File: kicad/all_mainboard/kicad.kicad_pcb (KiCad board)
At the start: 2 copper layers, 266 x 95 mm, 133 parts

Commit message: added kicad files
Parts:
- added D1: D,Zener,IEC, Diode_THT:D_DO-41_SOD81_P10.16mm_Horizontal, B.Cu at (127.4, 57.0)
- added D2: D,Zener,IEC, Diode_THT:D_DO-41_SOD81_P10.16mm_Horizontal, B.Cu at (131.4, 60.5)
- added J1: USB_A, custom:PinHeader_1x04_P2.00mm_Horizontal, F.Cu at (131.5, 26.0)
- added R1: 68R, Diode_THT:D_DO-41_SOD81_P10.16mm_Horizontal, B.Cu at (128.0, 84.4)
- added R2: 68R, Diode_THT:D_DO-41_SOD81_P10.16mm_Horizontal, B.Cu at (130.5, 71.4)
- added R3: 1k5, Diode_THT:D_DO-41_SOD81_P10.16mm_Horizontal, B.Cu at (111.5, 81.4)
- moved A2 157.4 mm to (122.9, 108.1), turned to -90 degrees
- moved D-2-13 25.3 mm to (266.7, 54.5), turned to 0 degrees
- moved D-4-6 9.79 mm to (141.0, 96.7), turned to -90 degrees
- moved D-0-10 8.24 mm to (209.7, 25.9), turned to 0 degrees
- moved D-0-11 8.24 mm to (228.7, 25.9), turned to 0 degrees
- moved D-0-12 8.24 mm to (247.7, 25.9), turned to 0 degrees
- moved D-0-13 8.24 mm to (266.7, 25.9), turned to 0 degrees
- moved D-0-2 8.24 mm to (57.7, 25.9), turned to 0 degrees
- moved D-0-3 8.24 mm to (76.7, 25.9), turned to 0 degrees
- moved D-0-4 8.24 mm to (95.7, 25.9), turned to 0 degrees
- moved D-0-5 8.24 mm to (114.7, 25.9), turned to 0 degrees
- moved D-0-7 8.24 mm to (152.7, 25.9), turned to 0 degrees
- moved D-0-8 8.24 mm to (171.7, 25.9), turned to 0 degrees
- moved D-0-9 8.24 mm to (190.7, 25.9), turned to 0 degrees
- moved D-1-10 8.24 mm to (209.7, 44.9), turned to 0 degrees
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- renumbered D-4-5 to D-4-6, D-4-8 to D-4-7, SW-4-5 to SW-4-6, SW-4-8 to SW-4-7
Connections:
- A2 pad A0: unconnected-(A2-PadA0) -> /tiny+ switch array standard/wr-4
- A2 pad A1: /tiny+ switch array standard/r-13 -> /tiny+ switch array standard/r-4
- A2 pad A2: /tiny+ switch array standard/r-12 -> /tiny+ switch array standard/r-0
- A2 pad A3: /tiny+ switch array standard/r-11 -> /tiny+ switch array standard/r-1
- A2 pad A4: /tiny+ switch array standard/r-10 -> /tiny+ switch array standard/r-3
- A2 pad A5: /tiny+ switch array standard/r-9 -> /tiny+ switch array standard/r-2
- A2 pad A6: /tiny+ switch array standard/r-8 -> /tiny+ switch array standard/r-9
- A2 pad A7: /tiny+ switch array standard/r-7 -> /tiny+ switch array standard/r-10
- A2 pad D1: /tiny+ switch array standard/r-6 -> /tiny+ switch array standard/wr-0
- A2 pad D10: /tiny+ switch array standard/wr-1 -> /tiny+ switch array standard/r-11
- A2 pad D11: /tiny+ switch array standard/wr-2 -> /tiny+ switch array standard/r-12
- A2 pad D12: /tiny+ switch array standard/wr-3 -> /tiny+ switch array standard/r-13
- A2 pad D13: /tiny+ switch array standard/wr-4 -> unconnected-(A2-D13_SCK-PadD13)
- A2 pad D2: unconnected-(A2-D2_INT0-PadD2) -> /tiny+ switch array standard/wr-1
- A2 pad D3: /tiny+ switch array standard/r-4 -> Net-(A2-D3_INT1)
- A2 pad D4: unconnected-(A2-PadD4) -> Net-(A2-PadD4)
- A2 pad D5: /tiny+ switch array standard/r-3 -> /tiny+ switch array standard/wr-3
- A2 pad D6: /tiny+ switch array standard/r-2 -> /tiny+ switch array standard/r-6
- A2 pad D7: /tiny+ switch array standard/r-1 -> /tiny+ switch array standard/wr-2
- A2 pad D8: /tiny+ switch array standard/r-0 -> /tiny+ switch array standard/r-7
- A2 pad D9: /tiny+ switch array standard/wr-0 -> /tiny+ switch array standard/r-8
- A2 pad GND1: unconnected-(A2-GND-PadGND1) -> Net-(D1-A+)
- A2 pad Vcc1: unconnected-(A2-Vcc-PadVcc1) -> Net-(A2-Vcc)
- D-4-6 pad 1: /tiny+ switch array standard/r-5 -> /tiny+ switch array standard/r-6
- D-4-6 pad 2: Net-(D-4-5-A) -> Net-(D-4-6-A)
- D-4-7 pad 1: /tiny+ switch array standard/r-8 -> /tiny+ switch array standard/r-7
- D-4-7 pad 2: Net-(D-4-8-A) -> Net-(D-4-7-A)
- SW-0-0 pad 1: /tiny+ switch array standard/wr-0 -> Net-(D-0-0-A)
- SW-0-0 pad 2: Net-(D-0-0-A) -> /tiny+ switch array standard/wr-0
- SW-0-1 pad 1: /tiny+ switch array standard/wr-0 -> Net-(D-0-1-A)
- SW-0-1 pad 2: Net-(D-0-1-A) -> /tiny+ switch array standard/wr-0
- SW-0-10 pad 1: /tiny+ switch array standard/wr-0 -> Net-(D-0-10-A)
- SW-0-10 pad 2: Net-(D-0-10-A) -> /tiny+ switch array standard/wr-0
- SW-0-11 pad 1: /tiny+ switch array standard/wr-0 -> Net-(D-0-11-A)
- SW-0-11 pad 2: Net-(D-0-11-A) -> /tiny+ switch array standard/wr-0
- SW-0-12 pad 1: /tiny+ switch array standard/wr-0 -> Net-(D-0-12-A)
- SW-0-12 pad 2: Net-(D-0-12-A) -> /tiny+ switch array standard/wr-0
- SW-0-13 pad 1: /tiny+ switch array standard/wr-0 -> Net-(D-0-13-A)
- SW-0-13 pad 2: Net-(D-0-13-A) -> /tiny+ switch array standard/wr-0
- SW-0-2 pad 1: /tiny+ switch array standard/wr-0 -> Net-(D-0-2-A)
- SW-0-2 pad 2: Net-(D-0-2-A) -> /tiny+ switch array standard/wr-0
- SW-0-3 pad 1: /tiny+ switch array standard/wr-0 -> Net-(D-0-3-A)
- SW-0-3 pad 2: Net-(D-0-3-A) -> /tiny+ switch array standard/wr-0
- SW-0-4 pad 1: /tiny+ switch array standard/wr-0 -> Net-(D-0-4-A)
- SW-0-4 pad 2: Net-(D-0-4-A) -> /tiny+ switch array standard/wr-0
- SW-0-5 pad 1: /tiny+ switch array standard/wr-0 -> Net-(D-0-5-A)
- SW-0-5 pad 2: Net-(D-0-5-A) -> /tiny+ switch array standard/wr-0
- SW-0-6 pad 1: /tiny+ switch array standard/wr-0 -> Net-(D-0-6-A)
- SW-0-6 pad 2: Net-(D-0-6-A) -> /tiny+ switch array standard/wr-0
- SW-0-7 pad 1: /tiny+ switch array standard/wr-0 -> Net-(D-0-7-A)
- SW-0-7 pad 2: Net-(D-0-7-A) -> /tiny+ switch array standard/wr-0
- SW-0-8 pad 1: /tiny+ switch array standard/wr-0 -> Net-(D-0-8-A)
- SW-0-8 pad 2: Net-(D-0-8-A) -> /tiny+ switch array standard/wr-0
- SW-0-9 pad 1: /tiny+ switch array standard/wr-0 -> Net-(D-0-9-A)
- SW-0-9 pad 2: Net-(D-0-9-A) -> /tiny+ switch array standard/wr-0
- SW-1-0 pad 1: /tiny+ switch array standard/wr-1 -> Net-(D-1-0-A)
- SW-1-0 pad 2: Net-(D-1-0-A) -> /tiny+ switch array standard/wr-1
- SW-1-1 pad 1: /tiny+ switch array standard/wr-1 -> Net-(D-1-1-A)
- SW-1-1 pad 2: Net-(D-1-1-A) -> /tiny+ switch array standard/wr-1
- SW-1-10 pad 1: /tiny+ switch array standard/wr-1 -> Net-(D-1-10-A)
- SW-1-10 pad 2: Net-(D-1-10-A) -> /tiny+ switch array standard/wr-1
- SW-1-11 pad 1: /tiny+ switch array standard/wr-1 -> Net-(D-1-11-A)
- SW-1-11 pad 2: Net-(D-1-11-A) -> /tiny+ switch array standard/wr-1
- SW-1-12 pad 1: /tiny+ switch array standard/wr-1 -> Net-(D-1-12-A)
- SW-1-12 pad 2: Net-(D-1-12-A) -> /tiny+ switch array standard/wr-1
- SW-1-2 pad 1: /tiny+ switch array standard/wr-1 -> Net-(D-1-2-A)
- SW-1-2 pad 2: Net-(D-1-2-A) -> /tiny+ switch array standard/wr-1
- SW-1-3 pad 1: /tiny+ switch array standard/wr-1 -> Net-(D-1-3-A)
- SW-1-3 pad 2: Net-(D-1-3-A) -> /tiny+ switch array standard/wr-1
- SW-1-4 pad 1: /tiny+ switch array standard/wr-1 -> Net-(D-1-4-A)
- SW-1-4 pad 2: Net-(D-1-4-A) -> /tiny+ switch array standard/wr-1
- SW-1-5 pad 1: /tiny+ switch array standard/wr-1 -> Net-(D-1-5-A)
- SW-1-5 pad 2: Net-(D-1-5-A) -> /tiny+ switch array standard/wr-1
- SW-1-6 pad 1: /tiny+ switch array standard/wr-1 -> Net-(D-1-6-A)
- SW-1-6 pad 2: Net-(D-1-6-A) -> /tiny+ switch array standard/wr-1
- SW-1-7 pad 1: /tiny+ switch array standard/wr-1 -> Net-(D-1-7-A)
- SW-1-7 pad 2: Net-(D-1-7-A) -> /tiny+ switch array standard/wr-1
- SW-1-8 pad 1: /tiny+ switch array standard/wr-1 -> Net-(D-1-8-A)
- SW-1-8 pad 2: Net-(D-1-8-A) -> /tiny+ switch array standard/wr-1
- SW-1-9 pad 1: /tiny+ switch array standard/wr-1 -> Net-(D-1-9-A)
- SW-1-9 pad 2: Net-(D-1-9-A) -> /tiny+ switch array standard/wr-1
- SW-2-0 pad 1: /tiny+ switch array standard/wr-2 -> Net-(D-2-0-A)
- SW-2-0 pad 2: Net-(D-2-0-A) -> /tiny+ switch array standard/wr-2
- SW-2-1 pad 1: /tiny+ switch array standard/wr-2 -> Net-(D-2-1-A)
- SW-2-1 pad 2: Net-(D-2-1-A) -> /tiny+ switch array standard/wr-2
- SW-2-10 pad 1: /tiny+ switch array standard/wr-2 -> Net-(D-2-10-A)
- SW-2-10 pad 2: Net-(D-2-10-A) -> /tiny+ switch array standard/wr-2
- SW-2-11 pad 1: /tiny+ switch array standard/wr-2 -> Net-(D-2-11-A)
- SW-2-11 pad 2: Net-(D-2-11-A) -> /tiny+ switch array standard/wr-2
- SW-2-12 pad 1: /tiny+ switch array standard/wr-2 -> Net-(D-2-12-A)
- SW-2-12 pad 2: Net-(D-2-12-A) -> /tiny+ switch array standard/wr-2
- SW-2-13 pad 1: /tiny+ switch array standard/wr-2 -> Net-(D-2-13-A)
- SW-2-13 pad 2: Net-(D-2-13-A) -> /tiny+ switch array standard/wr-2
- SW-2-2 pad 1: /tiny+ switch array standard/wr-2 -> Net-(D-2-2-A)
- SW-2-2 pad 2: Net-(D-2-2-A) -> /tiny+ switch array standard/wr-2
- SW-2-3 pad 1: /tiny+ switch array standard/wr-2 -> Net-(D-2-3-A)
- SW-2-3 pad 2: Net-(D-2-3-A) -> /tiny+ switch array standard/wr-2
- SW-2-4 pad 1: /tiny+ switch array standard/wr-2 -> Net-(D-2-4-A)
- SW-2-4 pad 2: Net-(D-2-4-A) -> /tiny+ switch array standard/wr-2
- SW-2-5 pad 1: /tiny+ switch array standard/wr-2 -> Net-(D-2-5-A)
- SW-2-5 pad 2: Net-(D-2-5-A) -> /tiny+ switch array standard/wr-2
- SW-2-6 pad 1: /tiny+ switch array standard/wr-2 -> Net-(D-2-6-A)
- SW-2-6 pad 2: Net-(D-2-6-A) -> /tiny+ switch array standard/wr-2
- SW-2-7 pad 1: /tiny+ switch array standard/wr-2 -> Net-(D-2-7-A)
- SW-2-7 pad 2: Net-(D-2-7-A) -> /tiny+ switch array standard/wr-2
- SW-2-8 pad 1: /tiny+ switch array standard/wr-2 -> Net-(D-2-8-A)
- SW-2-8 pad 2: Net-(D-2-8-A) -> /tiny+ switch array standard/wr-2
- SW-2-9 pad 1: /tiny+ switch array standard/wr-2 -> Net-(D-2-9-A)
- SW-2-9 pad 2: Net-(D-2-9-A) -> /tiny+ switch array standard/wr-2
- SW-3-0 pad 1: /tiny+ switch array standard/wr-3 -> Net-(D-3-0-A)
- SW-3-0 pad 2: Net-(D-3-0-A) -> /tiny+ switch array standard/wr-3
- SW-3-1 pad 1: /tiny+ switch array standard/wr-3 -> Net-(D-3-1-A)
- SW-3-1 pad 2: Net-(D-3-1-A) -> /tiny+ switch array standard/wr-3
- SW-3-10 pad 1: /tiny+ switch array standard/wr-3 -> Net-(D-3-10-A)
- SW-3-10 pad 2: Net-(D-3-10-A) -> /tiny+ switch array standard/wr-3
- SW-3-11 pad 1: /tiny+ switch array standard/wr-3 -> Net-(D-3-11-A)
- SW-3-11 pad 2: Net-(D-3-11-A) -> /tiny+ switch array standard/wr-3
- SW-3-12 pad 1: /tiny+ switch array standard/wr-3 -> Net-(D-3-12-A)
- SW-3-12 pad 2: Net-(D-3-12-A) -> /tiny+ switch array standard/wr-3
- SW-3-13 pad 1: /tiny+ switch array standard/wr-3 -> Net-(D-3-13-A)
- SW-3-13 pad 2: Net-(D-3-13-A) -> /tiny+ switch array standard/wr-3
- SW-3-2 pad 1: /tiny+ switch array standard/wr-3 -> Net-(D-3-2-A)
- SW-3-2 pad 2: Net-(D-3-2-A) -> /tiny+ switch array standard/wr-3
- SW-3-3 pad 1: /tiny+ switch array standard/wr-3 -> Net-(D-3-3-A)
- SW-3-3 pad 2: Net-(D-3-3-A) -> /tiny+ switch array standard/wr-3
- SW-3-4 pad 1: /tiny+ switch array standard/wr-3 -> Net-(D-3-4-A)
- SW-3-4 pad 2: Net-(D-3-4-A) -> /tiny+ switch array standard/wr-3
- SW-3-5 pad 1: /tiny+ switch array standard/wr-3 -> Net-(D-3-5-A)
- SW-3-5 pad 2: Net-(D-3-5-A) -> /tiny+ switch array standard/wr-3
- SW-3-6 pad 1: /tiny+ switch array standard/wr-3 -> Net-(D-3-6-A)
- SW-3-6 pad 2: Net-(D-3-6-A) -> /tiny+ switch array standard/wr-3
- SW-3-7 pad 1: /tiny+ switch array standard/wr-3 -> Net-(D-3-7-A)
- SW-3-7 pad 2: Net-(D-3-7-A) -> /tiny+ switch array standard/wr-3
- SW-3-8 pad 1: /tiny+ switch array standard/wr-3 -> Net-(D-3-8-A)
- SW-3-8 pad 2: Net-(D-3-8-A) -> /tiny+ switch array standard/wr-3
- SW-3-9 pad 1: /tiny+ switch array standard/wr-3 -> Net-(D-3-9-A)
- SW-3-9 pad 2: Net-(D-3-9-A) -> /tiny+ switch array standard/wr-3
- SW-4-0 pad 1: /tiny+ switch array standard/wr-4 -> Net-(D-4-0-A)
- SW-4-0 pad 2: Net-(D-4-0-A) -> /tiny+ switch array standard/wr-4
- SW-4-1 pad 1: /tiny+ switch array standard/wr-4 -> Net-(D-4-1-A)
- SW-4-1 pad 2: Net-(D-4-1-A) -> /tiny+ switch array standard/wr-4
- SW-4-10 pad 1: /tiny+ switch array standard/wr-4 -> Net-(D-4-10-A)
- SW-4-10 pad 2: Net-(D-4-10-A) -> /tiny+ switch array standard/wr-4
- SW-4-11 pad 1: /tiny+ switch array standard/wr-4 -> Net-(D-4-11-A)
- SW-4-11 pad 2: Net-(D-4-11-A) -> /tiny+ switch array standard/wr-4
- SW-4-12 pad 1: /tiny+ switch array standard/wr-4 -> Net-(D-4-12-A)
- SW-4-12 pad 2: Net-(D-4-12-A) -> /tiny+ switch array standard/wr-4
- SW-4-13 pad 1: /tiny+ switch array standard/wr-4 -> Net-(D-4-13-A)
- SW-4-13 pad 2: Net-(D-4-13-A) -> /tiny+ switch array standard/wr-4
- SW-4-2 pad 1: /tiny+ switch array standard/wr-4 -> Net-(D-4-2-A)
- SW-4-2 pad 2: Net-(D-4-2-A) -> /tiny+ switch array standard/wr-4
- SW-4-3 pad 1: /tiny+ switch array standard/wr-4 -> Net-(D-4-3-A)
- SW-4-3 pad 2: Net-(D-4-3-A) -> /tiny+ switch array standard/wr-4
- SW-4-6 pad 1: /tiny+ switch array standard/wr-4 -> Net-(D-4-6-A)
- SW-4-6 pad 2: Net-(D-4-5-A) -> /tiny+ switch array standard/wr-4
- SW-4-7 pad 1: /tiny+ switch array standard/wr-4 -> Net-(D-4-7-A)
- SW-4-7 pad 2: Net-(D-4-8-A) -> /tiny+ switch array standard/wr-4
- SW-4-9 pad 1: /tiny+ switch array standard/wr-4 -> Net-(D-4-9-A)
- SW-4-9 pad 2: Net-(D-4-9-A) -> /tiny+ switch array standard/wr-4
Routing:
- net /tiny+ switch array standard/r-1: track 344.6 -> 175.0 mm
- net /tiny+ switch array standard/r-0: track 363.1 -> 200.3 mm
- net /tiny+ switch array standard/r-5: track 242.2 -> 79.6 mm
- net /tiny+ switch array standard/r-2: track 309.7 -> 148.6 mm, vias 2 -> 0
- net /tiny+ switch array standard/r-3: track 287.0 -> 133.7 mm, vias 3 -> 0
- net /tiny+ switch array standard/r-13: track 95.5 -> 224.5 mm
- net /tiny+ switch array standard/r-4: track 238.9 -> 114.1 mm
- net Net-(A2-Vcc): track 0.00 -> 124.4 mm, vias 0 -> 2
- net /tiny+ switch array standard/r-12: track 90.7 -> 205.3 mm
- net /tiny+ switch array standard/r-6: track 200.8 -> 96.5 mm
- net Net-(D1-A+): track 0.00 -> 101.2 mm, vias 0 -> 3
- net Net-(D2-K-): track 0.00 -> 73.9 mm
- net /tiny+ switch array standard/r-11: track 111.1 -> 179.9 mm
- net /tiny+ switch array standard/r-8: track 179.1 -> 111.4 mm
- net Net-(D1-K-): track 0.00 -> 59.4 mm
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
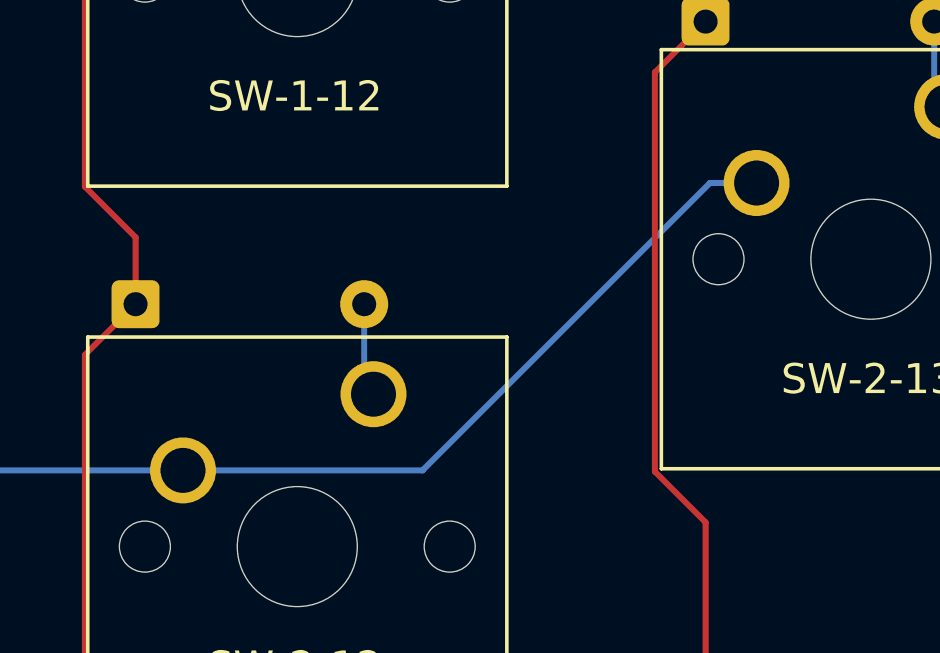
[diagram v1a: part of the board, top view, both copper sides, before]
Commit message: slight update to pcb to cross at 90 degrees
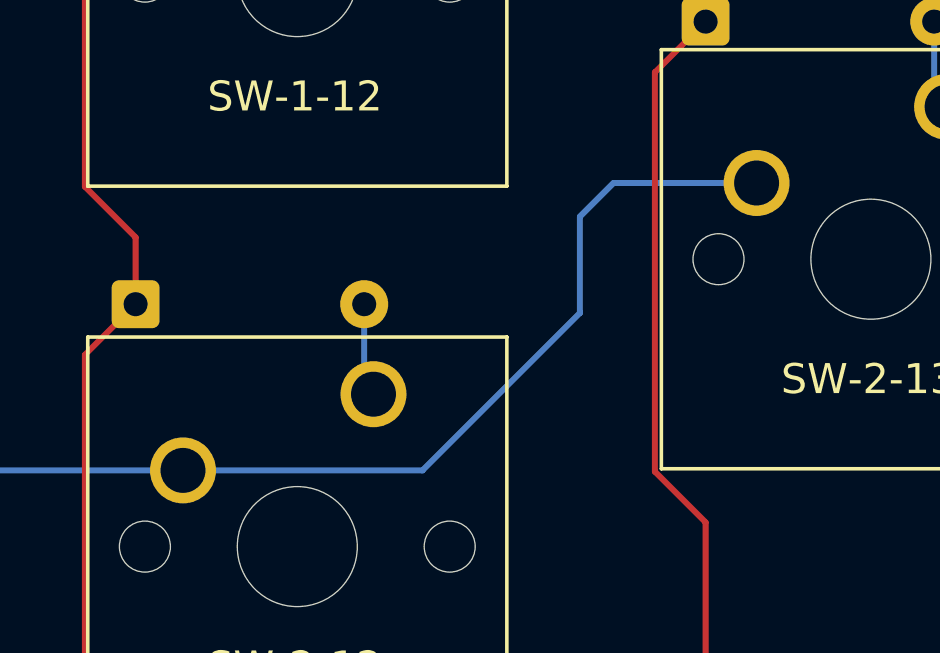
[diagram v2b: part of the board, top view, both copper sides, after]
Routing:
- net /tiny+ switch array standard/wr-2: track 285.3 -> 287.1 mm
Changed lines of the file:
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@@
-	)
-	(segment
-		(start 268.39 59.88)
-		(end 266.834366 59.88)
-		(width 0.2)
-		(layer "B.Cu")
-		(net 10)
 	)
 	(segment
@@
 	)
 	(segment
-		(start 257.254366 69.46)
-		(end 249.27 69.46)
+		(start 230.16 69.46)
+		(end 230.12 69.42)
 		(width 0.2)
 		(layer "B.Cu")
@@
 	)
 	(segment
-		(start 230.16 69.46)
-		(end 230.12 69.42)
+		(start 257.254366 69.46)
+		(end 262.5 64.214366)
 		(width 0.2)
 		(layer "B.Cu")
@@
 	)
 	(segment
-		(start 266.834366 59.88)
-		(end 257.254366 69.46)
+		(start 262.5 61)
+		(end 263.62 59.88)
 		(width 0.2)
 		(layer "B.Cu")
@@
 		(start 40.31 69.42)
 		(end 40.27 69.46)
+		(width 0.2)
+		(layer "B.Cu")
+		(net 10)
+	)
+	(segment
+		(start 263.62 59.88)
+		(end 268.39 59.88)
 		(width 0.2)
 		(layer "B.Cu")
@@
 		(start 59.12 69.42)
 		(end 40.31 69.42)
+		(width 0.2)
+		(layer "B.Cu")
+		(net 10)
+	)
+	(segment
+		(start 262.5 64.214366)
+		(end 262.5 61)
 		(width 0.2)
 		(layer "B.Cu")
@@
 		(width 0.2)
 		(layer "B.Cu")
+		(net 10)
+	)
+	(segment
+		(start 249.27 69.46)
+		(end 257.254366 69.46)
+		(width 0.2)
+		(layer "B.Cu")
